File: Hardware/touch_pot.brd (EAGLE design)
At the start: 44.5 x 78.7 mm, 78 parts, among them CON1 SINGLE_PADSMD, CON10 SINGLE_PADSMD, CON11 SINGLE_PADSMD, CON12 SINGLE_PADSMD, CON13 SINGLE_PADSMD, CON14 SINGLE_PADSMD, CON15 SINGLE_PADSMD, CON16 SINGLE_PADSMD_R, CON17 SINGLE_PADSMD_R, CON18 SINGLE_PADSMD_R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

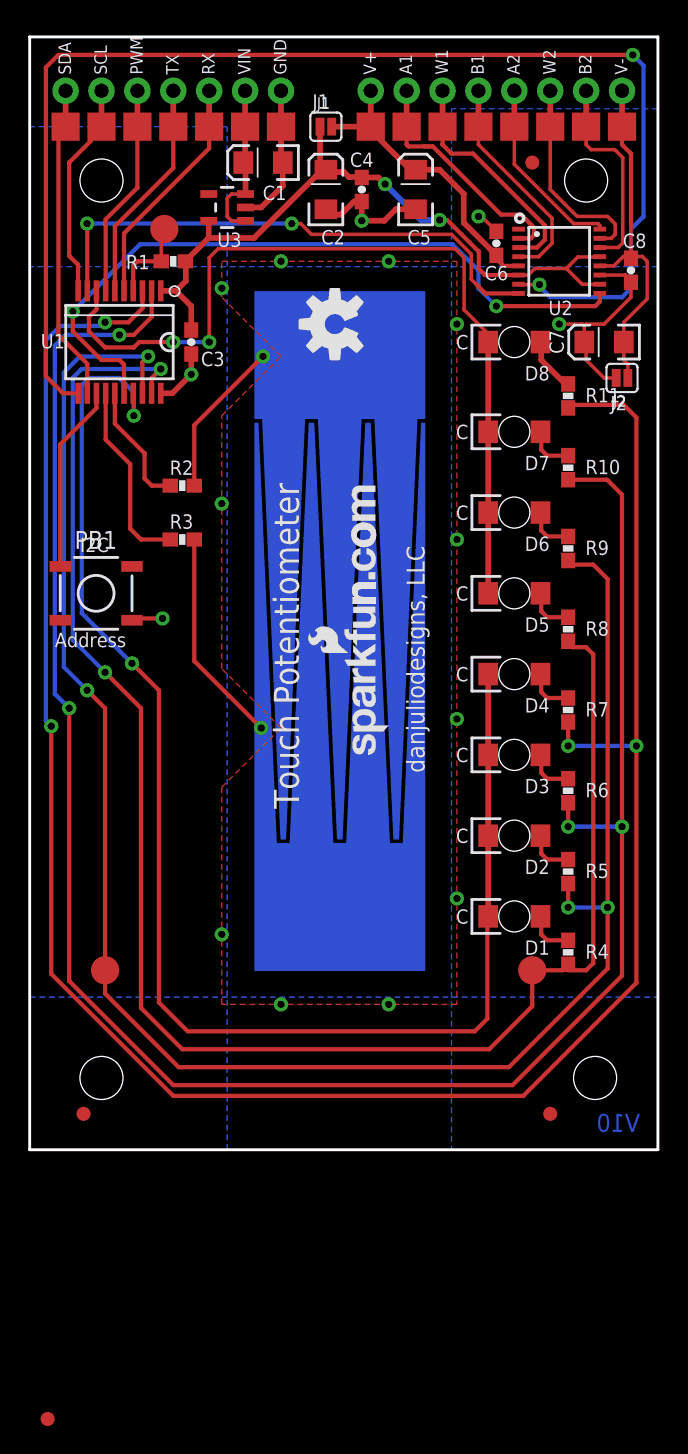
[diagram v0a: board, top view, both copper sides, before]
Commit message: 2nd Round of Protos
Added a few test points, moved a cap closer to analog IC, moved button
down to avoid touching resistors.
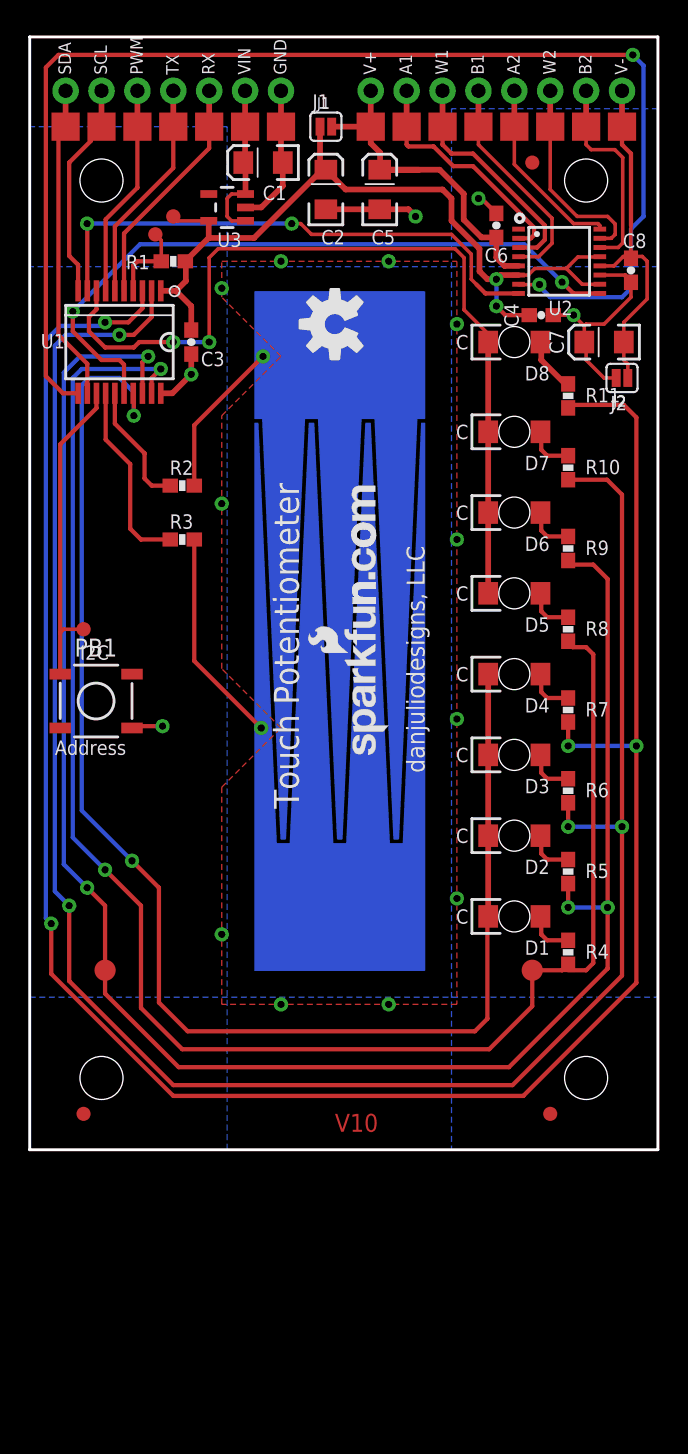
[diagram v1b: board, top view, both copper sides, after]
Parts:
- removed CON16: SINGLE_PADSMD_R, djd_eagle_library:2MM_R_SMD_PAD
- removed U$5: FIDUCIAL, djd_eagle_library:FIDUCIAL
- added TP1, TP2, TP3: (no value), SparkFun-Passives:PAD.03X.04
- CON17, CON18: value SINGLE_PADSMD_R -> SINGLE_PADSMD_R15; device djd_eagle_library:2MM_R_SMD_PAD -> djd_eagle_library:1_5MM_R_SMD_PAD
- moved C4 15.5 mm to (36.2, 59.1), turned to 0 degrees
- moved PB1 7.62 mm to (4.70, 31.8)
- moved C5 2.54 mm to (24.8, 67.9)
- moved C6 1.27 mm to (33.0, 65.4)
- moved STANDOFF4 0.64 mm to (39.4, 5.08)
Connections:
- net +5V: now also TP2.P$1
- net AUX: now also TP3.P$1
- net VPP: now also TP1.P$1; no longer CON16.P$1
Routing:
- net AUX: track 13.3 -> 22.7 mm
- net +5V: track 50.7 -> 59.3 mm
- net V+: track 22.6 -> 26.0 mm
- net CSN: track 50.6 -> 48.7 mm
- net GND: track 42.2 -> 41.6 mm
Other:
- board text added: "Joel Bartlett"

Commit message: Final commit before 2nd round of protos - 4 real
made all test points the same size, trace clean up, moved filtering cap
as close as possible.
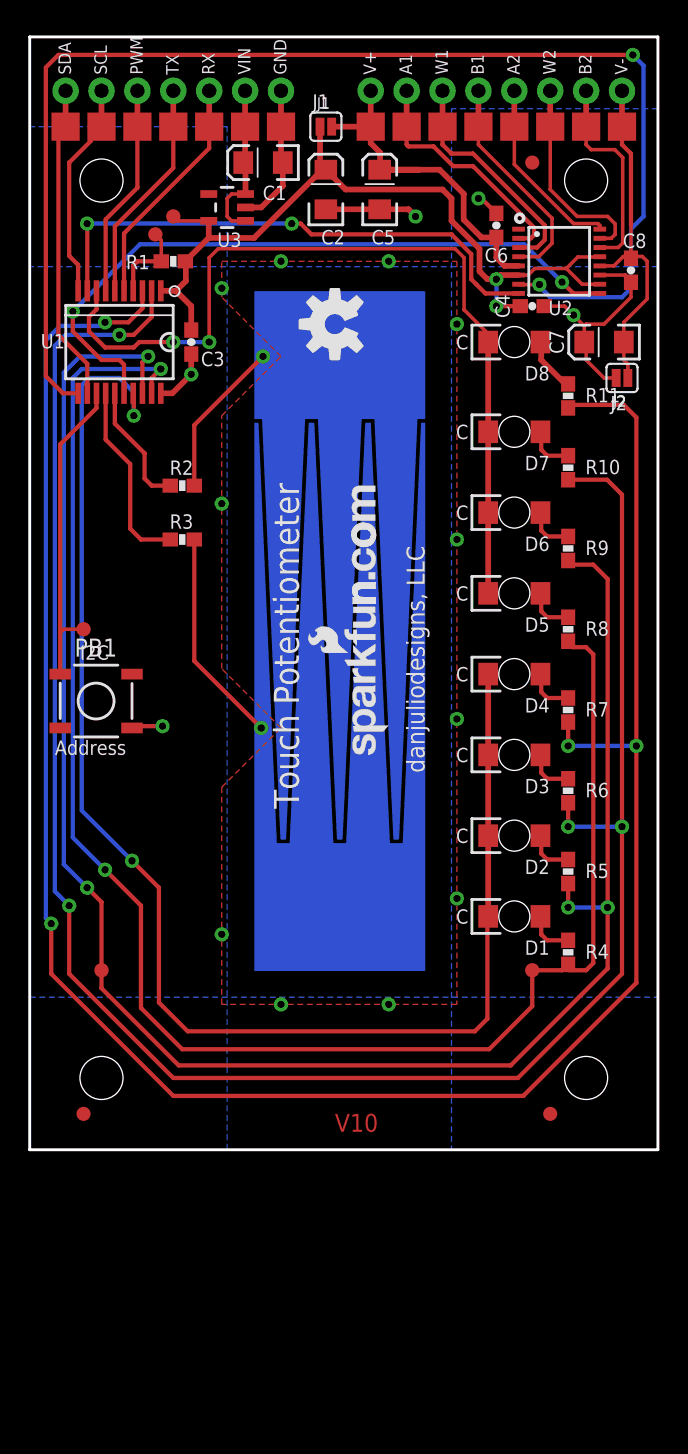
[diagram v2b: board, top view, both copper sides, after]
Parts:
- removed CON17, CON18: SINGLE_PADSMD_R15, djd_eagle_library:1_5MM_R_SMD_PAD
- added TP4, TP5: (no value), SparkFun-Passives:PAD.03X.04
- moved C4 0.90 mm to (35.6, 59.7)
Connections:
- net LA0: now also TP4.P$1; no longer CON17.P$1
- net LA1: now also TP5.P$1; no longer CON18.P$1
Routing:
- net GND: track 41.6 -> 42.5 mm
- net +5V: track 59.3 -> 58.4 mm
- net LA2: track 144.1 -> 143.3 mm
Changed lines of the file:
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@@
 <setting verticaltext="up"/>
 </settings>
-<grid distance="0.05" unitdist="inch" unit="inch" style="lines" multiple="1" display="yes" altdistance="0.005" altunitdist="inch" altunit="inch"/>
+<grid distance="0.025" unitdist="inch" unit="inch" style="lines" multiple="1" display="yes" altdistance="0.005" altunitdist="inch" altunit="inch"/>
 <layers>
 <layer number="1" name="Top" color="4" fill="1" visible="yes" active="yes"/>
@@
 <attribute name="VALUE" x="9.144" y="58.239" size="1.016" layer="27" font="vector" rot="R270"/>
 </element>
-<element name="C4" library="djd_eagle_library" package="C0603" value="0.1 uF" x="36.195" y="59.055" smashed="yes">
-<attribute name="NAME" x="34.598" y="58.216" size="1.016" layer="25" font="vector" rot="R90"/>
-<attribute name="VALUE" x="35.106" y="56.769" size="1.016" layer="27" font="vector"/>
+<element name="C4" library="djd_eagle_library" package="C0603" value="0.1 uF" x="35.56" y="59.69" smashed="yes">
+<attribute name="NAME" x="33.963" y="58.851" size="1.016" layer="25" font="vector" rot="R90"/>
+<attribute name="VALUE" x="34.471" y="57.404" size="1.016" layer="27" font="vector"/>
 </element>
 <element name="C5" library="SparkFun" package="EIA3216" value="10 uF" x="24.765" y="67.945" smashed="yes" rot="R90">
@@
 <attribute name="VALUE" x="9.398" y="60.579" size="1.016" layer="27" font="vector"/>
 </element>
-<element name="CON17" library="djd_eagle_library" package="1_5MM_R_SMD_PAD" value="SINGLE_PADSMD_R15" x="35.56" y="12.7"/>
-<element name="CON18" library="djd_eagle_library" package="1_5MM_R_SMD_PAD" value="SINGLE_PADSMD_R15" x="5.334" y="12.7"/>
 <element name="R4" library="djd_eagle_library" package="R0603" value="100 ohm" x="38.1" y="13.97" smashed="yes" rot="R270">
 <attribute name="NAME" x="39.316" y="13.512" size="1.016" layer="25" font="vector"/>
@@
 <element name="TP3" library="SparkFun-Passives" package="PAD.03X.04" value="" x="3.81" y="36.83"/>
 <element name="TP1" library="SparkFun-Passives" package="PAD.03X.04" value="" x="8.89" y="64.77"/>
+<element name="TP4" library="SparkFun-Passives" package="PAD.03X.04" value="" x="35.56" y="12.7"/>
+<element name="TP5" library="SparkFun-Passives" package="PAD.03X.04" value="" x="5.08" y="12.7"/>
 </elements>
 <signals>
@@
 <wire x1="39.24" y1="58.29" x2="38.475" y2="59.055" width="0.254" layer="1"/>
 <wire x1="38.475" y1="59.055" x2="38.481" y2="59.055" width="0.254" layer="1"/>
-<wire x1="37.045" y1="59.055" x2="38.481" y2="59.055" width="0.254" layer="1"/>
+<wire x1="36.41" y1="59.69" x2="37.846" y2="59.69" width="0.254" layer="1"/>
+<wire x1="37.846" y1="59.69" x2="38.481" y2="59.055" width="0.254" layer="1"/>
 </signal>
 <signal name="VIN">
@@
 <wire x1="1.778" y1="18.288" x2="1.778" y2="56.896" width="0.3048" layer="16"/>
 <wire x1="2.794" y1="17.272" x2="1.778" y2="18.288" width="0.3048" layer="16"/>
-<wire x1="2.794" y1="11.938" x2="2.794" y2="17.272" width="0.3048" layer="1"/>
-<wire x1="10.16" y1="4.572" x2="2.794" y2="11.938" width="0.3048" layer="1"/>
-<wire x1="10.16" y1="4.572" x2="34.163" y2="4.572" width="0.3048" layer="1"/>
-<wire x1="34.163" y1="4.572" x2="41.91" y2="12.319" width="0.3048" layer="1"/>
+<wire x1="2.794" y1="12.446" x2="2.794" y2="17.272" width="0.3048" layer="1"/>
+<wire x1="10.16" y1="5.08" x2="2.794" y2="12.446" width="0.3048" layer="1"/>
+<wire x1="10.16" y1="5.08" x2="34.544" y2="5.08" width="0.3048" layer="1"/>
+<wire x1="34.544" y1="5.08" x2="41.91" y2="12.446" width="0.3048" layer="1"/>
 <wire x1="2.54" y1="57.658" x2="6.35" y2="57.658" width="0.3048" layer="16"/>
 <wire x1="38.1" y1="22.86" x2="38.1" y2="24.55" width="0.3048" layer="1"/>
 <wire x1="41.91" y1="22.86" x2="38.1" y2="22.86" width="0.3048" layer="16"/>
-<wire x1="41.91" y1="12.319" x2="41.91" y2="22.86" width="0.3048" layer="1"/>
+<wire x1="41.91" y1="12.446" x2="41.91" y2="22.86" width="0.3048" layer="1"/>
 <wire x1="41.91" y1="22.86" x2="41.91" y2="46.355" width="0.3048" layer="1"/>
 <wire x1="40.855" y1="47.41" x2="38.1" y2="47.41" width="0.3048" layer="1"/>
@@
 <wire x1="12.6699" y1="65.725" x2="10.475" y2="65.725" width="0.254" layer="1"/>
 <wire x1="10.475" y1="65.725" x2="10.16" y2="66.04" width="0.254" layer="1"/>
-<wire x1="35.345" y1="59.055" x2="33.655" y2="59.055" width="0.3048" layer="1"/>
-<wire x1="33.655" y1="59.055" x2="33.02" y2="59.69" width="0.3048" layer="1"/>
 <via x="33.02" y="59.69" extent="1-16" drill="0.508"/>
 <wire x1="33.02" y1="59.69" x2="33.02" y2="61.595" width="0.3048" layer="16"/>
@@
 <wire x1="31.8262" y1="62.1538" x2="32.385" y2="61.595" width="0.4064" layer="1"/>
 <wire x1="32.385" y1="61.595" x2="33.02" y2="61.595" width="0.4064" layer="1"/>
+<wire x1="34.71" y1="59.69" x2="33.02" y2="59.69" width="0.3048" layer="1"/>
 </signal>
 <signal name="LED_PWM1">
@@
 <contactref element="R9" pad="2"/>
 <contactref element="R5" pad="2"/>
-<contactref element="CON18" pad="P$1"/>
 <wire x1="7.975" y1="55.727" x2="7.975" y2="53.525" width="0.3048" layer="1"/>
 <wire x1="8.382" y1="56.134" x2="7.975" y2="55.727" width="0.3048" layer="1"/>
@@
 <wire x1="2.413" y1="20.193" x2="2.413" y2="54.991" width="0.3048" layer="16"/>
 <wire x1="4.064" y1="18.542" x2="2.413" y2="20.193" width="0.3048" layer="16"/>
-<wire x1="5.334" y1="11.049" x2="10.541" y2="5.842" width="0.3048" layer="1"/>
-<wire x1="10.541" y1="5.842" x2="33.909" y2="5.842" width="0.3048" layer="1"/>
-<wire x1="33.909" y1="5.842" x2="40.894" y2="12.827" width="0.3048" layer="1"/>
 <wire x1="38.1" y1="17.145" x2="38.1" y2="18.835" width="0.3048" layer="1"/>
 <wire x1="40.894" y1="17.145" x2="38.1" y2="17.145" width="0.3048" layer="16"/>
@@
 <wire x1="40.894" y1="40.386" x2="39.878" y2="41.402" width="0.3048" layer="1"/>
 <wire x1="39.878" y1="41.402" x2="38.293" y2="41.402" width="0.3048" layer="1"/>
-<wire x1="5.334" y1="11.049" x2="5.334" y2="12.7" width="0.3048" layer="1"/>
-<wire x1="5.334" y1="12.7" x2="5.334" y2="17.272" width="0.3048" layer="1"/>
-<wire x1="5.334" y1="17.272" x2="4.064" y2="18.542" width="0.3048" layer="1"/>
 <via x="8.382" y="56.134" extent="1-16" drill="0.508"/>
 <via x="4.064" y="18.542" extent="1-16" drill="0.508"/>
@@
 <wire x1="38.293" y1="41.402" x2="38.293" y2="41.502" width="0.3048" layer="1"/>
 <wire x1="38.293" y1="41.502" x2="38.1" y2="41.695" width="0.3048" layer="1"/>
+<contactref element="TP5" pad="P$1"/>
+<wire x1="5.08" y1="11.43" x2="5.08" y2="12.7" width="0.3048" layer="1"/>
+<wire x1="4.064" y1="18.542" x2="5.08" y2="17.526" width="0.3048" layer="1"/>
+<wire x1="5.08" y1="17.526" x2="5.08" y2="12.7" width="0.3048" layer="1"/>
+<wire x1="10.541" y1="5.969" x2="5.08" y2="11.43" width="0.3048" layer="1"/>
+<wire x1="10.541" y1="5.969" x2="34.036" y2="5.969" width="0.3048" layer="1"/>
+<wire x1="34.036" y1="5.969" x2="40.894" y2="12.827" width="0.3048" layer="1"/>
 </signal>
 <signal name="LA0">
@@
 <contactref element="R8" pad="2"/>
 <contactref element="R4" pad="2"/>
-<contactref element="CON17" pad="P$1"/>
 <wire x1="8.625" y1="54.599" x2="8.625" y2="53.525" width="0.3048" layer="1"/>
 <wire x1="9.271" y1="55.245" x2="8.625" y2="54.599" width="0.3048" layer="1"/>
@@
 <wire x1="38.1" y1="12.7" x2="39.37" y2="12.7" width="0.3048" layer="1"/>
 <wire x1="10.795" y1="7.112" x2="32.512" y2="7.112" width="0.3048" layer="1"/>
-<wire x1="35.56" y1="10.16" x2="35.56" y2="12.7" width="0.3048" layer="1"/>
 <wire x1="32.512" y1="7.112" x2="35.56" y2="10.16" width="0.3048" layer="1"/>
 <via x="9.271" y="55.245" extent="1-16" drill="0.508"/>
 <via x="5.334" y="19.812" extent="1-16" drill="0.508"/>
-<wire x1="35.56" y1="12.7" x2="37.68" y2="12.7" width="0.3048" layer="1"/>
 <wire x1="37.68" y1="12.7" x2="38.1" y2="13.12" width="0.3048" layer="1"/>
 <wire x1="38.42" y1="35.56" x2="38.42" y2="35.66" width="0.3048" layer="1"/>
 <wire x1="38.42" y1="35.66" x2="38.1" y2="35.98" width="0.3048" layer="1"/>
 <wire x1="38.1" y1="12.7" x2="38.1" y2="13.12" width="0.254" layer="1"/>
+<contactref element="TP4" pad="P$1"/>
+<wire x1="35.56" y1="10.16" x2="35.56" y2="12.7" width="0.3048" layer="1"/>
+<wire x1="35.56" y1="12.7" x2="37.68" y2="12.7" width="0.3048" layer="1"/>
 </signal>
 <signal name="N$37">
@@
 <via x="4.064" y="65.532" extent="1-16" drill="0.508"/>
 <via x="18.542" y="65.532" extent="1-16" drill="0.508"/>
-<wire x1="19.939" y1="64.77" x2="29.845" y2="64.77" width="0.254" layer="1"/>
-<wire x1="31.612" y1="61.225" x2="31.242" y2="61.595" width="0.254" layer="1"/>
-<wire x1="31.242" y1="61.595" x2="31.242" y2="63.373" width="0.254" layer="1"/>
-<wire x1="31.242" y1="63.373" x2="29.845" y2="64.77" width="0.254" layer="1"/>
+<wire x1="19.939" y1="64.77" x2="29.845" y2="64.77" width="0.3048" layer="1"/>
+<wire x1="31.612" y1="61.225" x2="31.242" y2="61.595" width="0.3048" layer="1"/>
+<wire x1="31.242" y1="61.595" x2="31.242" y2="63.373" width="0.3048" layer="1"/>
+<wire x1="31.242" y1="63.373" x2="29.845" y2="64.77" width="0.3048" layer="1"/>
 <wire x1="31.612" y1="61.225" x2="32.247" y2="60.59" width="0.3048" layer="1"/>
 <wire x1="32.247" y1="60.59" x2="34.59" y2="60.59" width="0.3048" layer="1"/>
-<wire x1="19.939" y1="64.77" x2="19.177" y2="65.532" width="0.254" layer="1"/>
-<wire x1="19.177" y1="65.532" x2="18.542" y2="65.532" width="0.254" layer="1"/>
+<wire x1="19.939" y1="64.77" x2="19.177" y2="65.532" width="0.3048" layer="1"/>
+<wire x1="19.177" y1="65.532" x2="18.542" y2="65.532" width="0.3048" layer="1"/>
 </signal>
 <signal name="CSN">
